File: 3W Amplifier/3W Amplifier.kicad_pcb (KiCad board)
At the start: 2 copper layers, 20 parts, among them SW1 SW_DIP_x02, U1 PAM8008

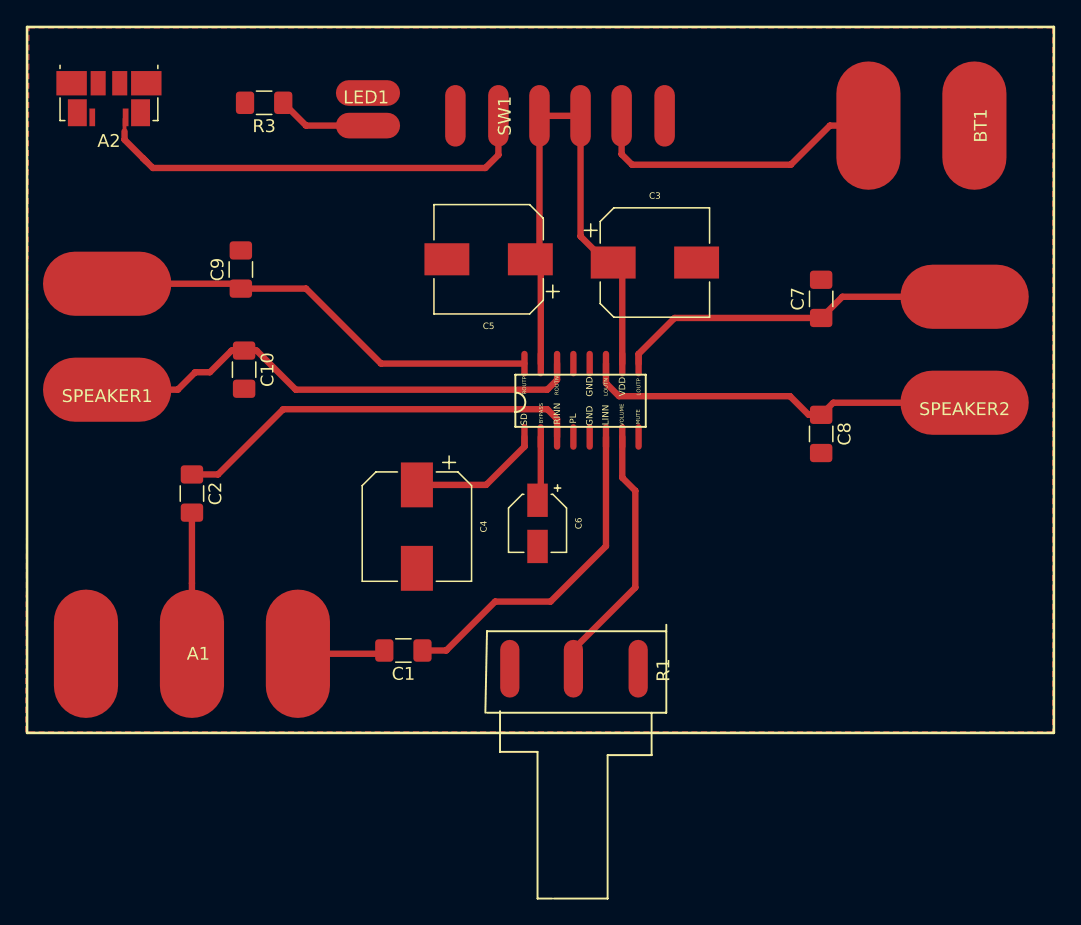
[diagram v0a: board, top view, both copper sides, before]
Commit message: have most of power routed
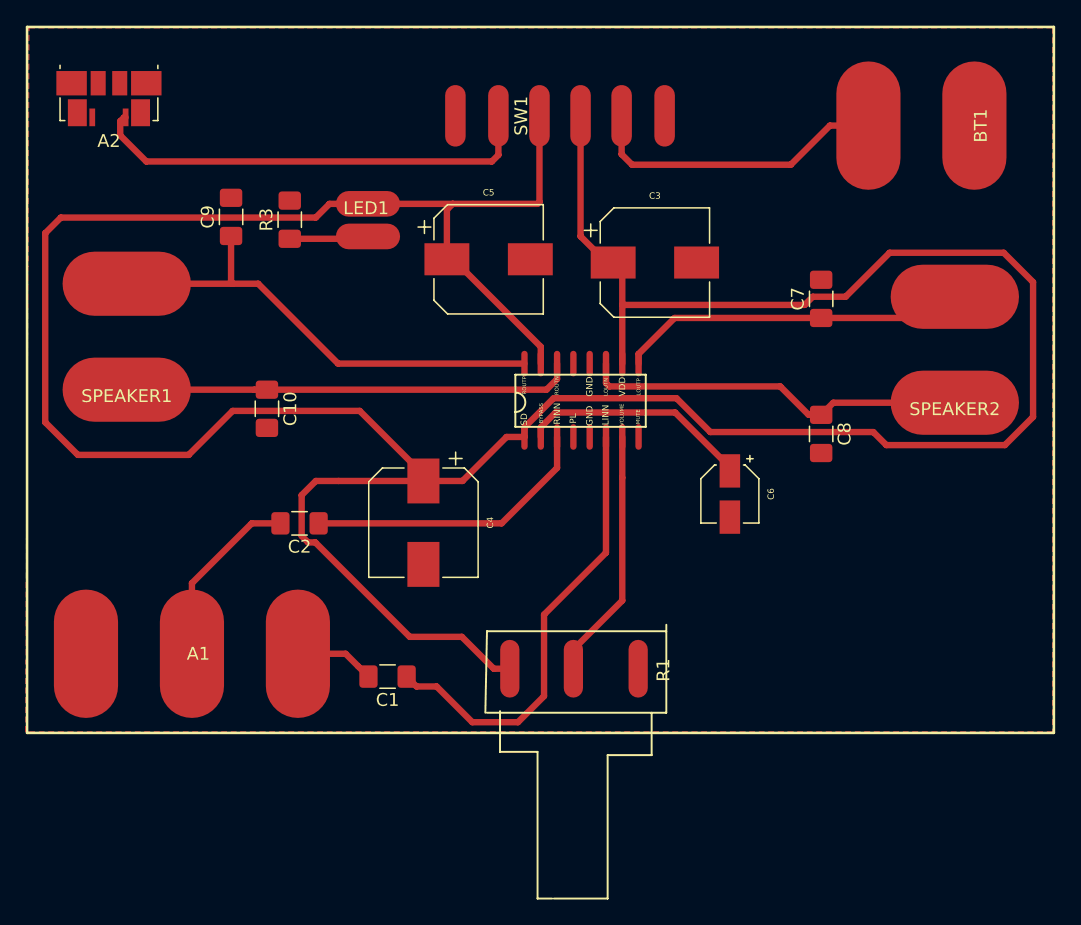
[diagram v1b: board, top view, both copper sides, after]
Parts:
- moved C6 15.2 mm to (79.8, 56.4)
- moved R3 9.32 mm to (45.5, 35.0), turned to 90 degrees
- moved C2 8.70 mm to (46.2, 58.7), turned to 180 degrees
- moved LED1 8.64 mm to (51.6, 36.3)
- moved C9 4.17 mm to (40.9, 34.8)
- moved C10 3.53 mm to (43.7, 49.7)
- moved C1 2.38 mm to (53.1, 70.6)
- moved SPEAKER1 1.52 mm to (32.8, 48.3)
- moved SPEAKER2 0.76 mm to (97.3, 49.3)
- moved C4 0.59 mm to (55.9, 58.6)
- turned C5 to 0 degrees
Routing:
- net /VDD: track 54.4 -> 264.1 mm
- net /BYPASS: track 5.04 -> 18.1 mm
- net /RINN: track 32.3 -> 22.8 mm
- net /LINN: track 26.2 -> 35.2 mm
- net /ROUTN: track 39.2 -> 35.5 mm
- net Net-(A1-PadR): track 11.0 -> 14.3 mm
- net /ROUTP: track 35.1 -> 37.3 mm
- net Net-(LED1-Pad1): track 7.34 -> 6.17 mm
- net /VOLUME: track 20.5 -> 19.6 mm

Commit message: Fully routed
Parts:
- moved A1 1.52 mm to (37.8, 67.3)
- moved SPEAKER2 1.27 mm to (96.0, 49.3)
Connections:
- A2 pad 1: (no net) -> Net-(A2-Pad1)
- SW1 pad 1: (no net) -> Net-(A2-Pad1)
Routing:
- net (no net): track 35.2 -> 0.00 mm
- net Net-(A2-Pad1): track 0.00 -> 34.6 mm
- net /VDD: track 264.1 -> 260.7 mm
- net /GND: track 0.00 -> 1.43 mm
- net /LINN: track 35.2 -> 35.8 mm

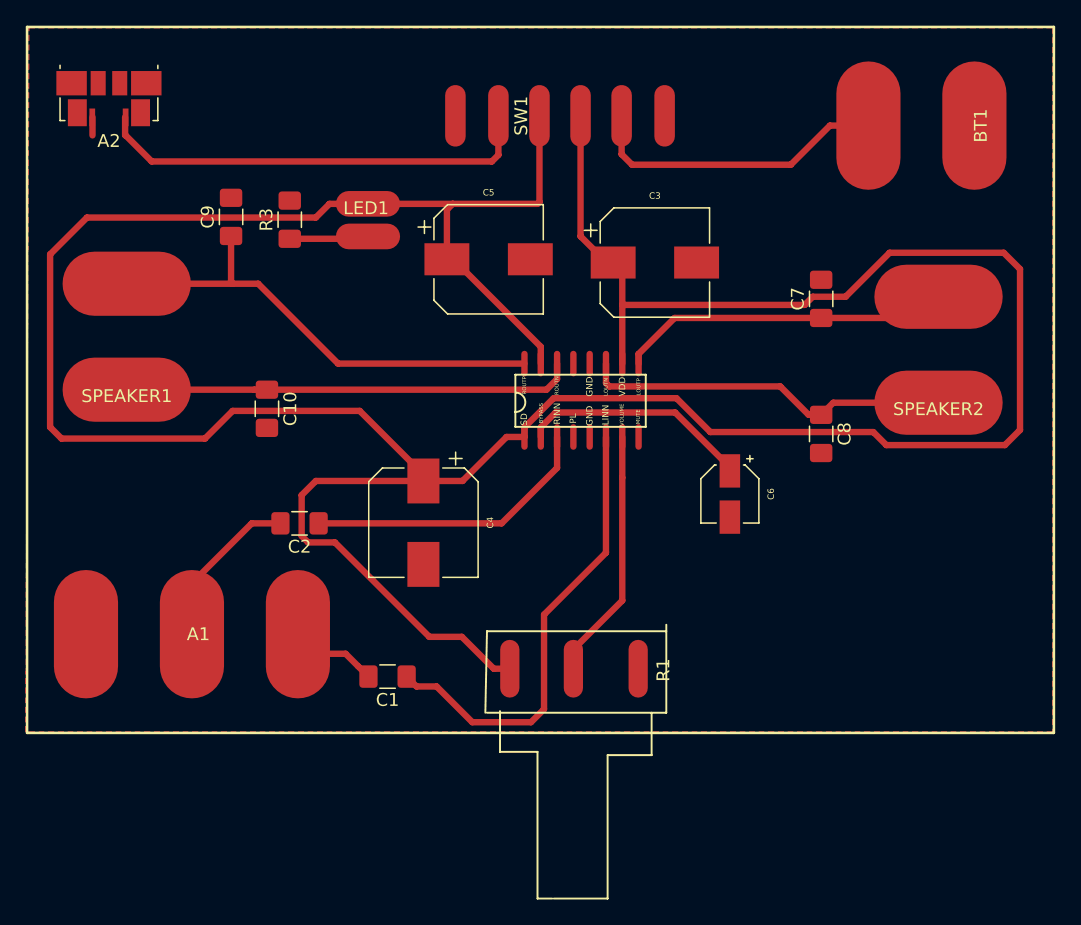
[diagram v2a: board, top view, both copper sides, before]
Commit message: Moved the led, moved the USB, added margin on the left and right
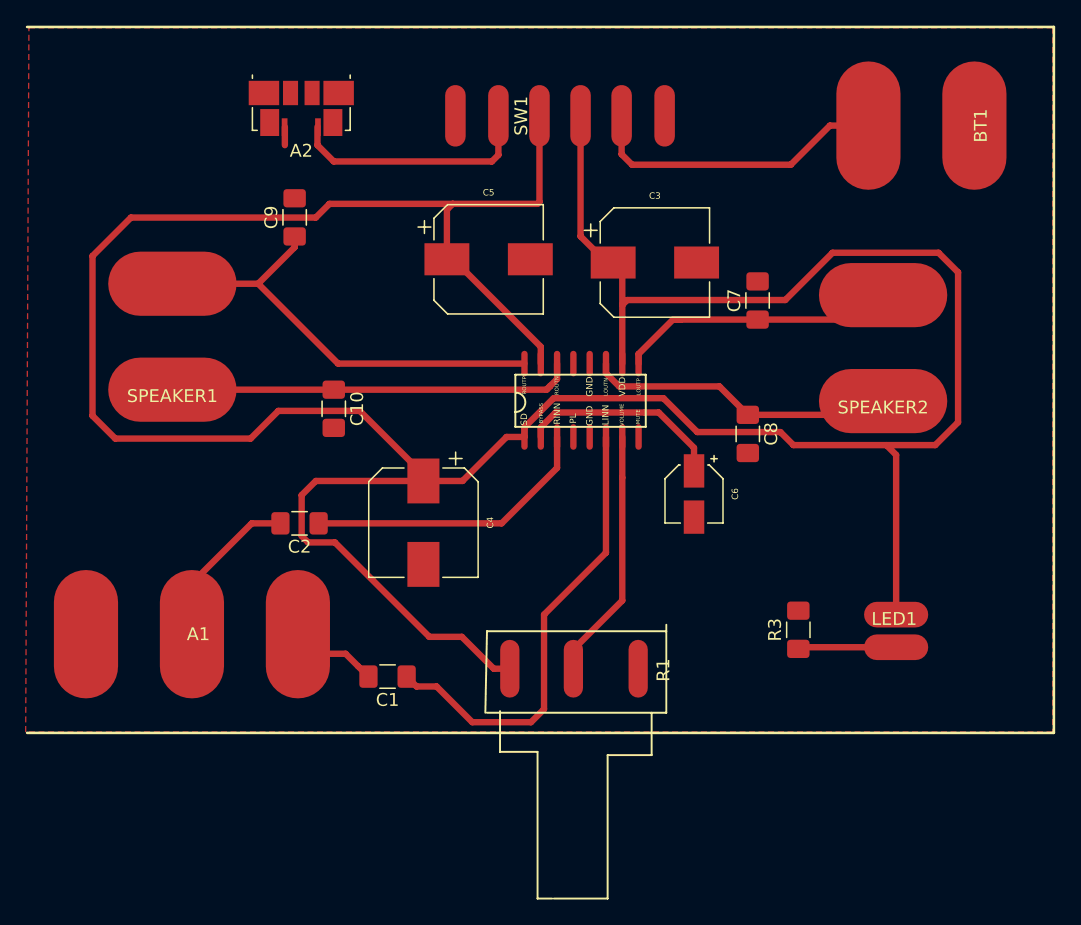
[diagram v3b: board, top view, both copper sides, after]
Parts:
- moved LED1 52.1 mm to (92.7, 68.3)
- moved R3 50.9 mm to (85.1, 67.0)
- moved A2 15.0 mm to (46.4, 26.3)
- moved C8 5.71 mm to (81.2, 51.7)
- moved C10 5.21 mm to (48.9, 49.7)
- moved C7 4.95 mm to (81.9, 41.3)
- moved C9 4.95 mm to (45.8, 34.8)
- moved SPEAKER2 4.32 mm to (91.7, 49.1)
- moved SPEAKER1 3.56 mm to (36.3, 48.3)
- moved C6 2.79 mm to (77.0, 56.4)
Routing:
- net Net-(A2-Pad1): track 34.6 -> 19.3 mm
- net /LOUTN: track 30.9 -> 24.1 mm
- net /LOUTP: track 28.0 -> 22.1 mm
- net /VDD: track 260.7 -> 256.9 mm
- net /ROUTN: track 35.5 -> 32.3 mm
- net /ROUTP: track 37.3 -> 34.9 mm
- net /BYPASS: track 18.1 -> 16.1 mm
- net Net-(LED1-Pad1): track 6.17 -> 7.67 mm

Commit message: rotate LED and move battery connector towards center
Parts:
- moved BT1 9.91 mm to (88.9, 27.7)
- moved LED1 2.62 mm to (90.2, 67.7), turned to 270 degrees
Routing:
- net Net-(BT1-Pad1): track 23.8 -> 13.9 mm
- net Net-(LED1-Pad1): track 7.67 -> 5.58 mm
- net /VDD: track 256.9 -> 258.8 mm
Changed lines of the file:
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@@
     (thickness 1.6)
     (drawings 3)
-    (tracks 121)
+    (tracks 122)
     (zones 0)
     (modules 20)
@@
     (mod_text_size 1 1)
     (mod_text_width 0.15)
-    (pad_size 1.425 1.75)
+    (pad_size 10 5)
     (pad_drill 0)
     (pad_to_mask_clearance 0.2)
@@
   )
   (module NewFootPrint:LED-Through-hole (layer F.Cu)
-    (at 92.71 68.326)
-    (fp_text reference LED1 (at -0.15 -2.202) (layer F.SilkS)
-      (effects (font (size 1 1) (thickness 0.15)))
-    )
-    (fp_text value GREEN (at -0.127 -6.774) (layer F.Fab)
-      (effects (font (size 1 1) (thickness 0.15)))
-    )
-    (pad 2 smd oval (at 0 -2.54) (size 5 2) (layers F.Cu F.Paste F.Mask)
+    (at 90.17 67.691 270)
+    (fp_text reference LED1 (at -0.15 -2.202 270) (layer F.SilkS)
+      (effects (font (size 1 1) (thickness 0.15)))
+    )
+    (fp_text value GREEN (at -0.127 -6.774 270) (layer F.Fab)
+      (effects (font (size 1 1) (thickness 0.15)))
+    )
+    (pad 2 smd oval (at 0 -2.54 270) (size 5 2) (layers F.Cu F.Paste F.Mask)
       (net 9 /VDD))
-    (pad 1 smd oval (at 0 0) (size 5 2) (layers F.Cu F.Paste F.Mask)
+    (pad 1 smd oval (at 0 0 270) (size 5 2) (layers F.Cu F.Paste F.Mask)
       (net 11 "Net-(LED1-Pad1)"))
   )
@@
   )
   (module NewFootPrint:Speaker (layer F.Cu)
-    (at 98.806 27.686 90)
+    (at 88.9 27.686 90)
     (fp_text reference BT1 (at 0 0.5 90) (layer F.SilkS)
       (effects (font (size 1 1) (thickness 0.15)))
@@
   (segment (start 46.896404 60.15901) (end 48.98301 60.15901) (width 0.5) (layer F.Cu) (net 9))
   (segment (start 48.98301 60.15901) (end 56.339 67.515) (width 0.5) (layer F.Cu) (net 9))
-  (segment (start 92.71 53.34) (end 91.948 52.578) (width 0.5) (layer F.Cu) (net 9))
-  (segment (start 92.71 65.786) (end 92.71 53.34) (width 0.5) (layer F.Cu) (net 9))
   (segment (start 44.57551 49.91249) (end 50.92049 49.91249) (width 0.5) (layer F.Cu) (net 9))
   (segment (start 42.418 52.07) (end 44.57551 49.91249) (width 0.5) (layer F.Cu) (net 9))
@@
   (segment (start 96.012 37.592) (end 97.536 39.116) (width 0.5) (layer F.Cu) (net 9))
   (segment (start 97.536 39.116) (end 97.536 50.8) (width 0.5) (layer F.Cu) (net 9))
+  (segment (start 92.71 53.34) (end 92.456 53.086) (width 0.5) (layer F.Cu) (net 9))
+  (segment (start 92.71 67.691) (end 92.71 53.34) (width 0.5) (layer F.Cu) (net 9))
+  (segment (start 92.456 53.086) (end 91.948 52.578) (width 0.5) (layer F.Cu) (net 9))
   (segment (start 45.974 68.707) (end 46.101 68.834) (width 0.5) (layer F.Cu) (net 10))
   (segment (start 49.8205 68.834) (end 50.8 69.8135) (width 0.5) (layer F.Cu) (net 10))
@@
   (segment (start 50.8 69.8135) (end 51.5985 70.612) (width 0.5) (layer F.Cu) (net 10))
   (segment (start 85.217 68.326) (end 85.09 68.453) (width 0.5) (layer F.Cu) (net 11))
-  (segment (start 92.71 68.326) (end 85.217 68.326) (width 0.5) (layer F.Cu) (net 11))
+  (segment (start 89.408 68.453) (end 90.17 67.691) (width 0.5) (layer F.Cu) (net 11))
+  (segment (start 85.09 68.453) (end 89.408 68.453) (width 0.5) (layer F.Cu) (net 11))
+  (segment (start 77.597 30.734) (end 80.645 27.686) (width 0.5) (layer F.Cu) (net 12))
+  (segment (start 72.136 30.734) (end 77.597 30.734) (width 0.5) (layer F.Cu) (net 12))
   (segment (start 71.322 26.924) (end 71.322 29.92) (width 0.5) (layer F.Cu) (net 12))
   (segment (start 71.322 29.92) (end 72.136 30.734) (width 0.5) (layer F.Cu) (net 12))
-  (segment (start 87.551 27.686) (end 90.551 27.686) (width 0.5) (layer F.Cu) (net 12))
-  (segment (start 84.503 30.734) (end 87.551 27.686) (width 0.5) (layer F.Cu) (net 12))
-  (segment (start 72.136 30.734) (end 84.503 30.734) (width 0.5) (layer F.Cu) (net 12))
   (segment (start 71.374 55.118) (end 71.374 51.943) (width 0.5) (layer F.Cu) (net 13))
   (segment (start 71.374 64.69) (end 71.374 55.118) (width 0.5) (layer F.Cu) (net 13))
